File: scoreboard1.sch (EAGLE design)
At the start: 0 parts

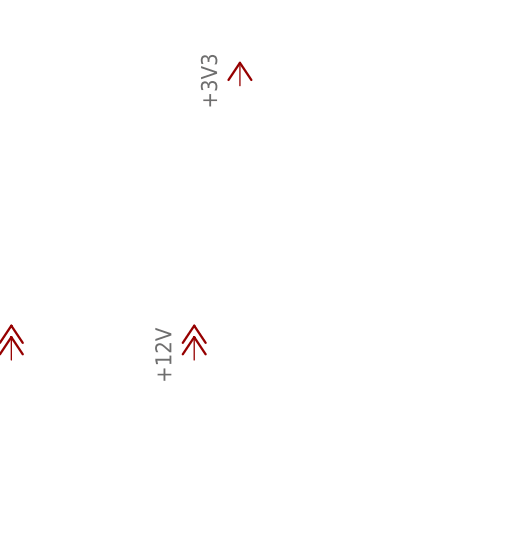
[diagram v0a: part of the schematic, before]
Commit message: created darlington array
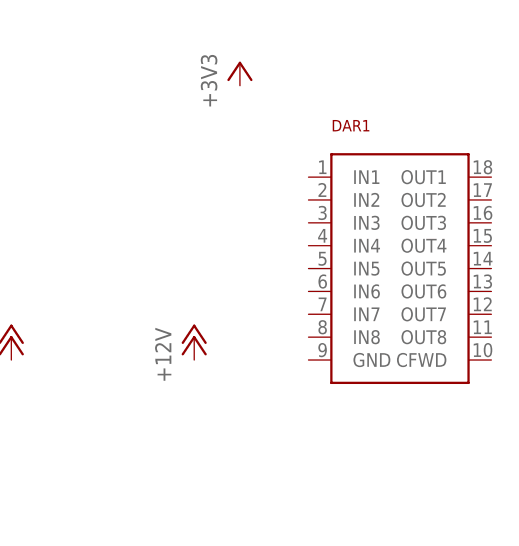
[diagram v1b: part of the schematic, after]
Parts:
- added DAR1: ULN2803A, ULN2803:ULN2803A
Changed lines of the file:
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@@
 <?xml version="1.0" encoding="utf-8"?>
 <!DOCTYPE eagle SYSTEM "eagle.dtd">
-<eagle version="7.2.0">
+<eagle version="7.6.0">
 <drawing>
 <settings>
@@
 <layer number="48" name="Document" color="7" fill="1" visible="no" active="no"/>
 <layer number="49" name="Reference" color="7" fill="1" visible="no" active="no"/>
+<layer number="50" name="dxf" color="7" fill="1" visible="no" active="no"/>
 <layer number="51" name="tDocu" color="7" fill="1" visible="no" active="no"/>
 <layer number="52" name="bDocu" color="7" fill="1" visible="no" active="no"/>
+<layer number="53" name="tGND_GNDA" color="7" fill="9" visible="no" active="no"/>
+<layer number="54" name="bGND_GNDA" color="1" fill="9" visible="no" active="no"/>
+<layer number="56" name="wert" color="7" fill="1" visible="no" active="no"/>
+<layer number="57" name="tCAD" color="7" fill="1" visible="no" active="no"/>
 <layer number="90" name="Modules" color="5" fill="1" visible="yes" active="yes"/>
 <layer number="91" name="Nets" color="2" fill="1" visible="yes" active="yes"/>
@@
 <layer number="97" name="Info" color="7" fill="1" visible="yes" active="yes"/>
 <layer number="98" name="Guide" color="6" fill="1" visible="yes" active="yes"/>
+<layer number="100" name="Muster" color="7" fill="1" visible="no" active="no"/>
+<layer number="101" name="Patch_Top" color="12" fill="4" visible="yes" active="yes"/>
+<layer number="102" name="Vscore" color="7" fill="1" visible="yes" active="yes"/>
+<layer number="103" name="fp3" color="7" fill="1" visible="no" active="yes"/>
+<layer number="104" name="Name" color="7" fill="1" visible="yes" active="yes"/>
+<layer number="105" name="Beschreib" color="9" fill="1" visible="yes" active="yes"/>
+<layer number="106" name="BGA-Top" color="4" fill="1" visible="yes" active="yes"/>
+<layer number="107" name="BD-Top" color="5" fill="1" visible="yes" active="yes"/>
+<layer number="108" name="fp8" color="7" fill="1" visible="no" active="yes"/>
+<layer number="109" name="fp9" color="7" fill="1" visible="no" active="yes"/>
+<layer number="110" name="fp0" color="7" fill="1" visible="no" active="yes"/>
+<layer number="111" name="LPC17xx" color="7" fill="1" visible="yes" active="yes"/>
+<layer number="112" name="tSilk" color="7" fill="1" visible="yes" active="yes"/>
+<layer number="116" name="Patch_BOT" color="9" fill="4" visible="yes" active="yes"/>
+<layer number="121" name="_tsilk" color="7" fill="1" visible="yes" active="yes"/>
+<layer number="122" name="_bsilk" color="7" fill="1" visible="yes" active="yes"/>
+<layer number="123" name="tTestmark" color="7" fill="1" visible="no" active="yes"/>
+<layer number="124" name="bTestmark" color="7" fill="1" visible="no" active="yes"/>
+<layer number="125" name="_tNames" color="7" fill="1" visible="yes" active="yes"/>
+<layer number="126" name="_bNames" color="7" fill="1" visible="yes" active="yes"/>
+<layer number="127" name="_tValues" color="7" fill="1" visible="yes" active="yes"/>
+<layer number="128" name="_bValues" color="7" fill="1" visible="yes" active="yes"/>
+<layer number="131" name="tAdjust" color="7" fill="1" visible="no" active="yes"/>
+<layer number="132" name="bAdjust" color="7" fill="1" visible="no" active="yes"/>
+<layer number="144" name="Drill_legend" color="7" fill="1" visible="yes" active="yes"/>
+<layer number="150" name="Notes" color="7" fill="1" visible="no" active="yes"/>
+<layer number="151" name="HeatSink" color="7" fill="1" visible="yes" active="yes"/>
+<layer number="152" name="_bDocu" color="7" fill="1" visible="yes" active="yes"/>
+<layer number="153" name="FabDoc1" color="6" fill="1" visible="no" active="no"/>
+<layer number="154" name="FabDoc2" color="2" fill="1" visible="no" active="no"/>
+<layer number="155" name="FabDoc3" color="7" fill="15" visible="no" active="no"/>
+<layer number="199" name="Contour" color="7" fill="1" visible="yes" active="yes"/>
+<layer number="200" name="200bmp" color="1" fill="10" visible="yes" active="yes"/>
+<layer number="201" name="201bmp" color="2" fill="1" visible="no" active="no"/>
+<layer number="202" name="202bmp" color="3" fill="1" visible="no" active="no"/>
+<layer number="203" name="203bmp" color="4" fill="10" visible="yes" active="yes"/>
+<layer number="204" name="204bmp" color="5" fill="10" visible="yes" active="yes"/>
+<layer number="205" name="205bmp" color="6" fill="10" visible="yes" active="yes"/>
+<layer number="206" name="206bmp" color="7" fill="10" visible="yes" active="yes"/>
+<layer number="207" name="207bmp" color="8" fill="10" visible="yes" active="yes"/>
+<layer number="208" name="208bmp" color="9" fill="10" visible="yes" active="yes"/>
+<layer number="209" name="209bmp" color="7" fill="1" visible="no" active="yes"/>
+<layer number="210" name="210bmp" color="7" fill="1" visible="no" active="yes"/>
+<layer number="211" name="211bmp" color="7" fill="1" visible="yes" active="yes"/>
+<layer number="212" name="212bmp" color="7" fill="1" visible="yes" active="yes"/>
+<layer number="213" name="213bmp" color="7" fill="1" visible="yes" active="yes"/>
+<layer number="214" name="214bmp" color="7" fill="1" visible="yes" active="yes"/>
+<layer number="215" name="215bmp" color="7" fill="1" visible="yes" active="yes"/>
+<layer number="216" name="216bmp" color="7" fill="1" visible="yes" active="yes"/>
+<layer number="217" name="217bmp" color="18" fill="1" visible="no" active="no"/>
+<layer number="218" name="218bmp" color="19" fill="1" visible="no" active="no"/>
+<layer number="219" name="219bmp" color="20" fill="1" visible="no" active="no"/>
+<layer number="220" name="220bmp" color="21" fill="1" visible="no" active="no"/>
+<layer number="221" name="221bmp" color="22" fill="1" visible="no" active="no"/>
+<layer number="222" name="222bmp" color="23" fill="1" visible="no" active="no"/>
+<layer number="223" name="223bmp" color="24" fill="1" visible="no" active="no"/>
+<layer number="224" name="224bmp" color="25" fill="1" visible="no" active="no"/>
+<layer number="248" name="Housing" color="7" fill="1" visible="yes" active="yes"/>
+<layer number="249" name="Edge" color="7" fill="1" visible="yes" active="yes"/>
+<layer number="250" name="Descript" color="7" fill="1" visible="no" active="no"/>
+<layer number="251" name="SMDround" color="7" fill="1" visible="no" active="no"/>
+<layer number="254" name="cooling" color="7" fill="1" visible="yes" active="yes"/>
 </layers>
 <schematic xreflabel="%F%N/%S.%C%R" xrefpart="/%S.%C%R">
@@
 <part name="GND3" library="supply1" deviceset="GND" device=""/>
 <part name="GND4" library="supply1" deviceset="GND" device=""/>
+<part name="DAR1" library="ULN2803" deviceset="ULN2803A" device=""/>
 </parts>
 <sheets>
@@
 <instance part="GND3" gate="1" x="88.9" y="15.24"/>
 <instance part="GND4" gate="1" x="109.22" y="17.78"/>
+<instance part="DAR1" gate="G$1" x="101.6" y="50.8"/>
 </instances>
 <busses>

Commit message: added stm parts, started sch design
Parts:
- added BOOT0, BOOT1: OMRON_B3U-1000P-B, omron_b3u:OMRON_B3U-1000P-B
- added C1, C2, C3, C4: .1 uF, passives_lean:0402_CAP_NON_POLAR
- added DAR2: ULN2803A, ULN2803:ULN2803A
- added MCU2: STM32F030C6TCTR, stm32f030:STM32F030C6TCTR
- added R-PI1: PI_ZERO_POWER_AND_GPIO, raspberry_pi_w:PI_ZERO_POWER_AND_GPIO
- added R1, R9: 10 kOhm, passives_lean:0402_RESISTOR
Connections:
- new net +3V3: BOOT1.IN, C1.1, C2.1, C3.1, C4.1, MCU2G$1.VDD1, MCU2G$1.VDD2, MCU2G$1.VDD3, MCU2G$1.VDDA, R-PI1G$1.3V3_1, R-PI1G$1.3V3_2, R9.2
- new net +5V: R-PI1G$1.5V_1, R-PI1G$1.5V_2
- new net GND: BOOT0.IN, C1.2, C2.2, C3.2, C4.2, DAR1.GND, DAR2.GND, MCU2G$1.VSS2, MCU2G$1.VSS3, MCU2G$1.VSSA, R-PI1G$1.GND1, R-PI1G$1.GND2, R-PI1G$1.GND3, R-PI1G$1.GND4, R-PI1G$1.GND5, R-PI1G$1.GND6, R-PI1G$1.GND7, R-PI1G$1.GND8, R1.2
- new net NRST: BOOT0.OUT, MCU2G$1.NRST, R9.1
- new net NRST1: BOOT1.OUT, MCU2G$1.BOOT0, R1.1
- new net RX1: MCU2G$2.PA10
- new net SWCLK: MCU2G$2.PA14
- new net SWDIO: MCU2G$2.PA13
- new net TX1: MCU2G$2.PA9
- new net VBUS: C1.1
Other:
- note added: "Darlington Arrays"
- note added: "LDO REGULATOR"
- note added: "Programming Port"
- note added: "Raspberry Pi GPIO Section"
- note added: "Raspberry Pi Power Section"
- note added: "STM PROGRAMMING HEADER"
- note added: "STM32F030 Logic"
- note added: "STM32F030 POWER AND CONFIG"
- note added: "Voltage Regulator"
